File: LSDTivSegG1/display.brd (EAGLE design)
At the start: 150 x 100 mm, 99 parts, among them IC1 MEGA8-P, IC2 MAX232, IC3 PCF8574P, IC4 PCF8574P, IC5 PCF8574P, IC6 PCF8574P

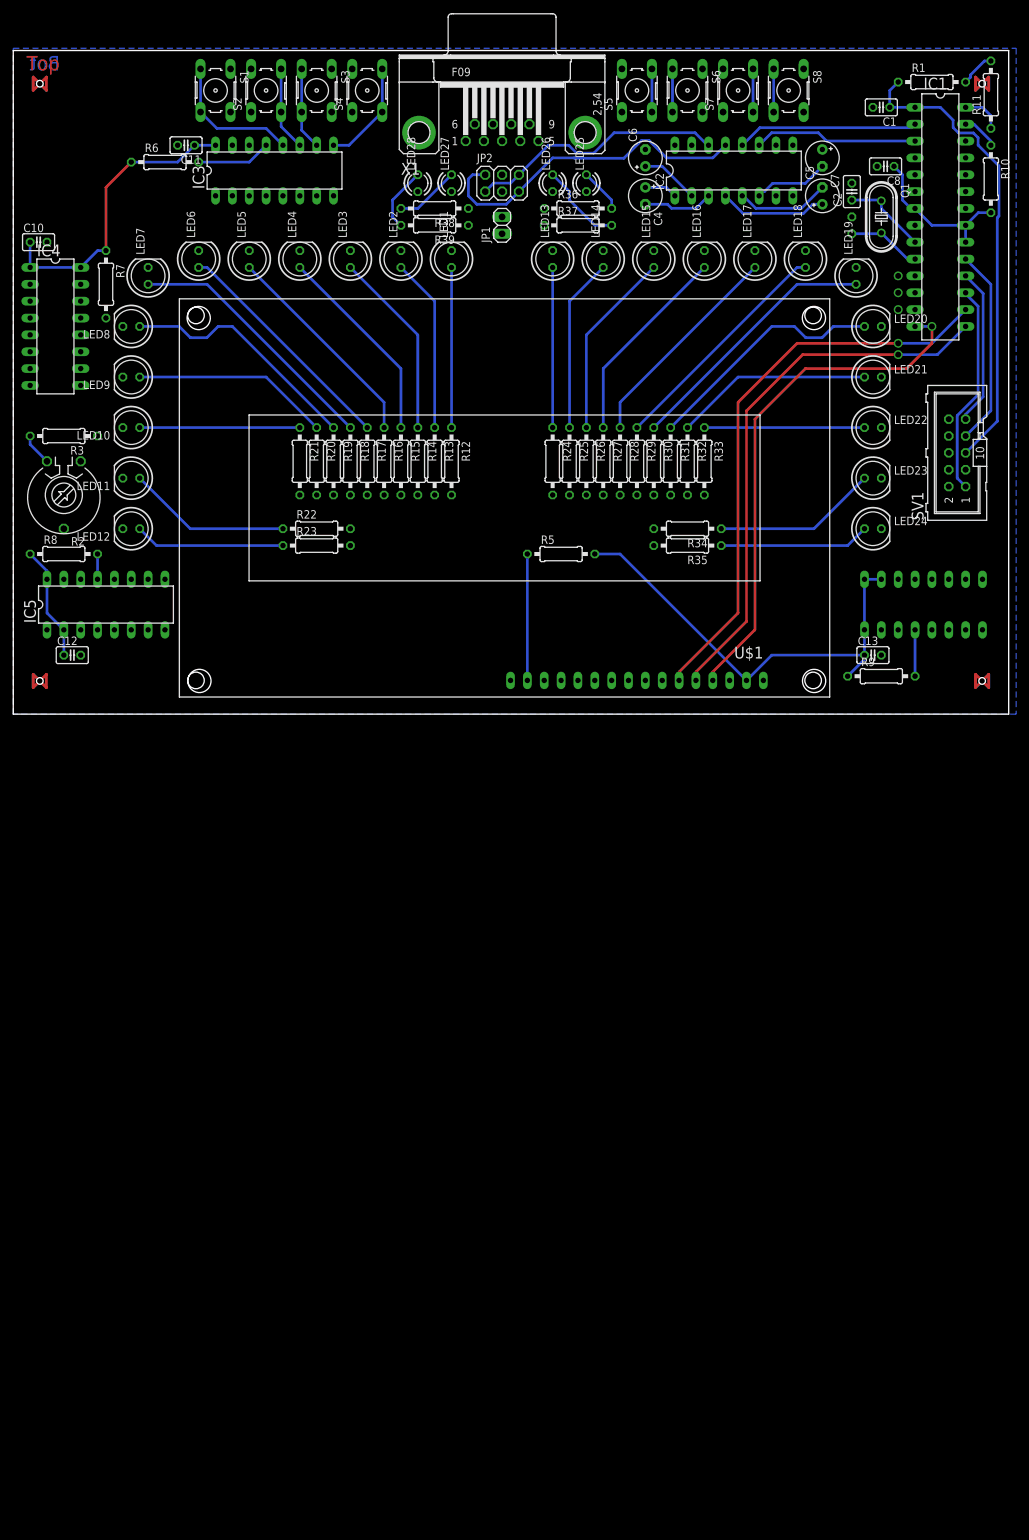
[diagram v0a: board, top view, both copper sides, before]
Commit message: worked on board layout (ca. 80% routed) changed LEDs from GND to +5V
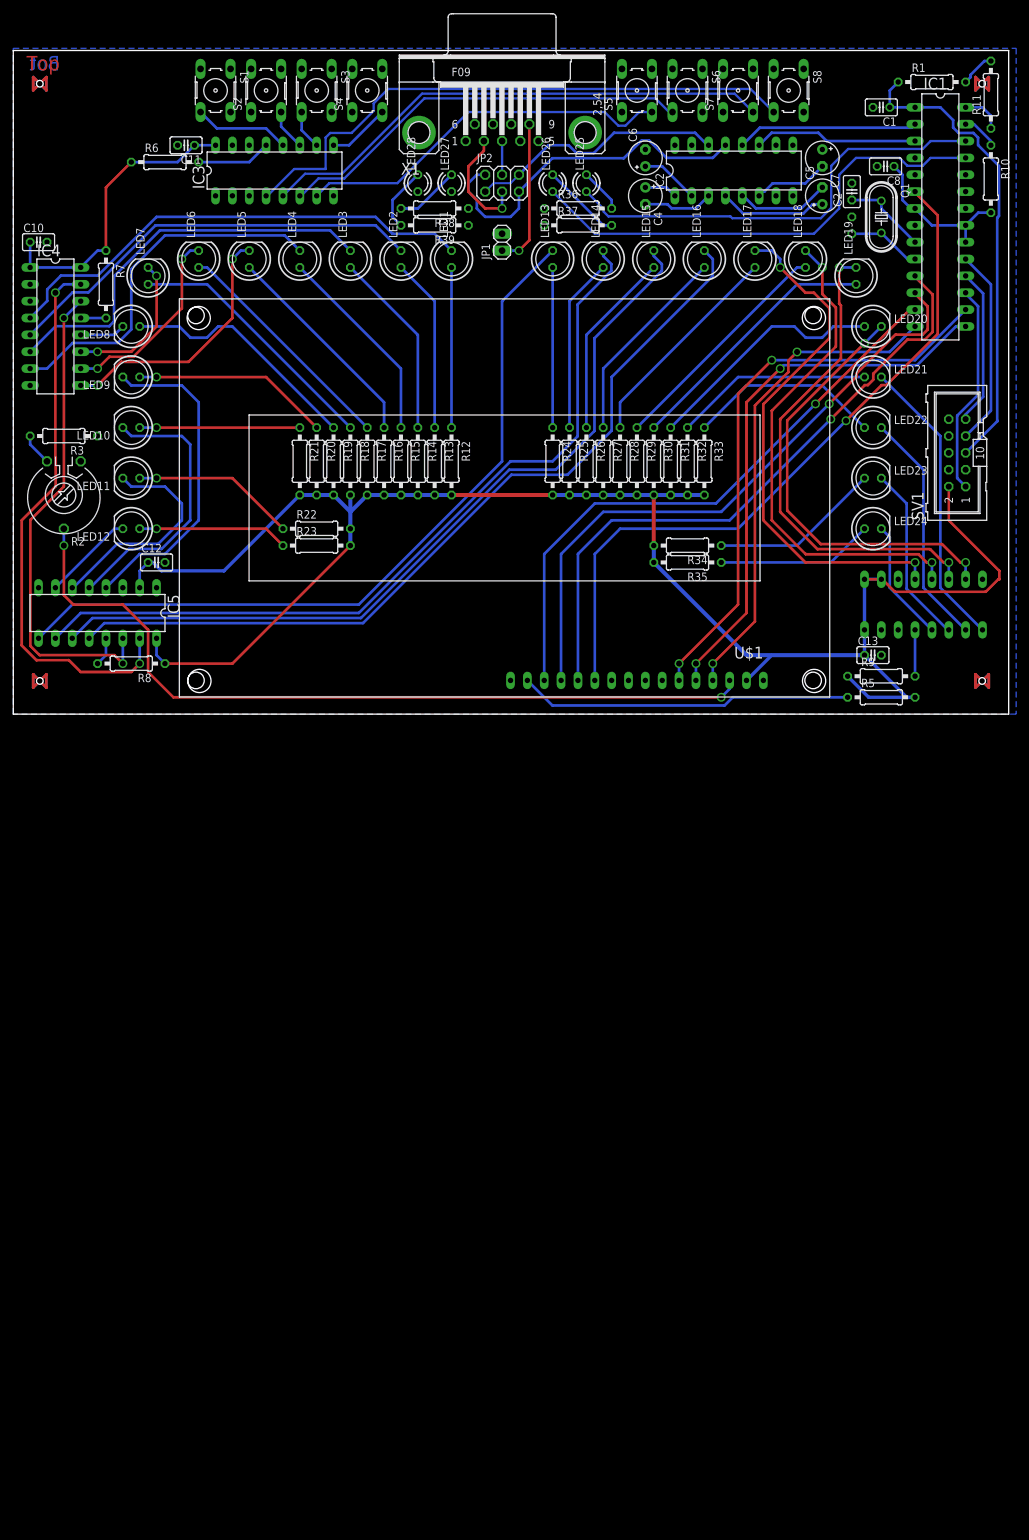
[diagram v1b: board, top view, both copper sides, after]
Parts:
- moved R5 52.9 mm to (130.8, 2.54)
- moved R8 19.4 mm to (17.8, 7.62), turned to 180 degrees
- moved C12 18.9 mm to (21.6, 22.9)
- moved R34 2.54 mm to (101.6, 25.4)
- moved R35 2.54 mm to (101.6, 22.9)
- moved JP1 2.54 mm to (73.7, 71.1)
- moved IC5 1.80 mm to (12.7, 15.2), turned to 180 degrees
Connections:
- net +5V: now also R12.2, R13.2, R14.2, R15.2, R16.2, R17.2, R18.2, R19.2, R20.2, R21.2, R22.2, R23.2, R24.2, R25.2, R26.2, R27.2, R28.2, R29.2, R30.2, R31.2, R32.2, R33.2, R34.2, R35.2
- net GND: no longer R12.2, R13.2, R14.2, R15.2, R16.2, R17.2, R18.2, R19.2, R20.2, R21.2, R22.2, R23.2, R24.2, R25.2, R26.2, R27.2, R28.2, R29.2, R30.2, R31.2, R32.2, R33.2, R34.2, R35.2
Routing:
- net +5V: track 159.8 -> 358.7 mm
- net LED15: track 0.00 -> 125.7 mm
- net LED14: track 0.00 -> 123.5 mm
- net N$10: track 0.00 -> 122.2 mm, vias 0 -> 2
- net LED13: track 0.00 -> 121.9 mm
- net LED12: track 0.00 -> 115.8 mm
- net D4: track 0.00 -> 107.3 mm, vias 0 -> 1
- net D5: track 0.00 -> 96.4 mm, vias 0 -> 1
- net D6: track 0.00 -> 94.9 mm, vias 0 -> 1
- net D7: track 0.00 -> 90.2 mm, vias 0 -> 1
- net SDA: track 6.13 -> 89.5 mm, vias 0 -> 2
- net BTN0: track 6.50 -> 88.0 mm
- net LED16: track 0.00 -> 79.7 mm, vias 0 -> 2
- net LED17: track 0.00 -> 75.8 mm, vias 0 -> 2
- net LED18: track 0.00 -> 74.4 mm, vias 0 -> 2
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
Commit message: added npn transistors to LED bars
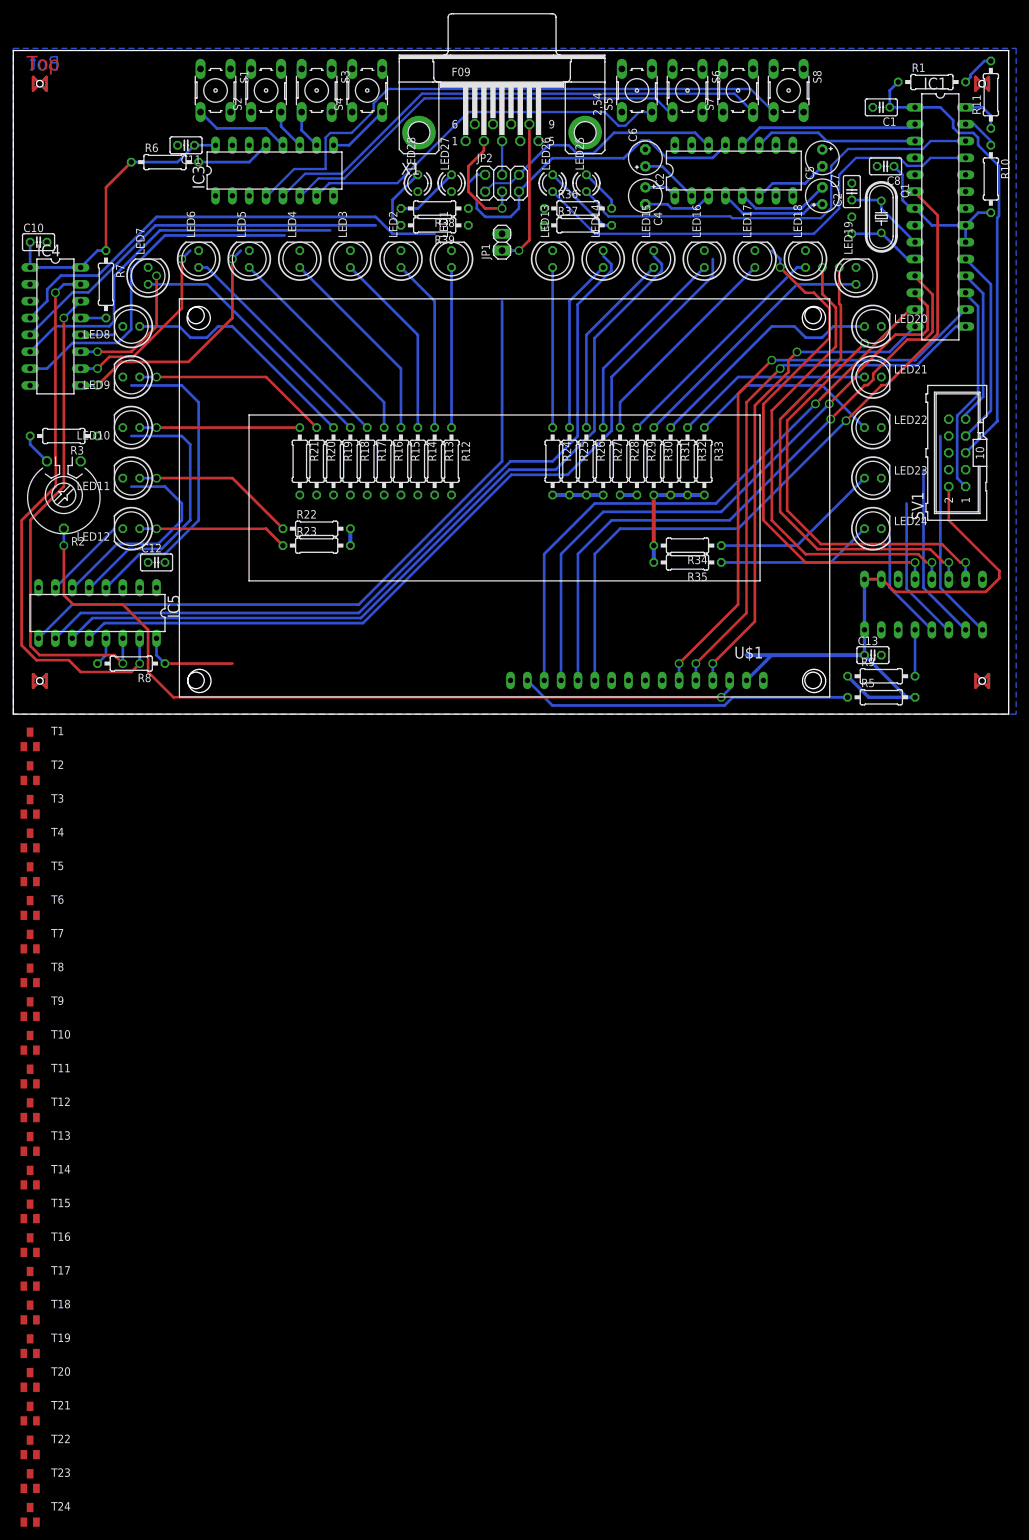
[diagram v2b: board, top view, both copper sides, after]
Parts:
- added T1, T10, T11, T12, T13, T14, T15, T16, T17, T18, T19, T2, T20, T21, T22, T23, T24, T3, T4, T5, T6, T7, T8, T9: BC847, transistor:SOT23
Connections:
- new net N$51: LED9.K, T9.3
- new net N$53: LED1.K, T1.3
- new net N$54: LED2.K, T2.3
- new net N$55: LED3.K, T3.3
- new net N$56: LED4.K, T4.3
- new net N$57: LED5.K, T5.3
- new net N$58: LED6.K, T6.3
- new net N$59: LED17.K, T17.3
- new net N$60: LED10.K, T10.3
- new net N$61: LED11.K, T11.3
- new net N$62: LED12.K, T12.3
- new net N$63: LED13.K, T13.3
- new net N$64: LED14.K, T14.3
- new net N$65: LED7.K, T7.3
- new net N$66: LED8.K, T8.3
- new net N$67: LED15.K, T15.3
- new net N$68: LED16.K, T16.3
- new net N$69: LED18.K, T18.3
- new net N$70: LED19.K, T19.3
- new net N$71: LED20.K, T20.3
- new net N$72: LED21.K, T21.3
- new net N$73: LED22.K, T22.3
- new net N$74: LED23.K, T23.3
- new net N$75: LED24.K, T24.3
- net GND: now also T1.2, T10.2, T11.2, T12.2, T13.2, T14.2, T15.2, T16.2, T17.2, T18.2, T19.2, T2.2, T20.2, T21.2, T22.2, T23.2, T24.2, T3.2, T4.2, T5.2, T6.2, T7.2, T8.2, T9.2
- net LED0: now also T1.1; no longer LED1.K
- net LED1: now also T2.1; no longer LED2.K
- net LED10: now also T11.1; no longer LED11.K
- net LED11: now also T12.1; no longer LED12.K
- net LED12: now also T13.1; no longer LED13.K
- net LED13: now also T14.1; no longer LED14.K
- net LED14: now also T15.1; no longer LED15.K
- net LED15: now also T16.1; no longer LED16.K
- net LED16: now also T17.1; no longer LED17.K
- net LED17: now also T18.1; no longer LED18.K
- net LED18: now also T19.1; no longer LED19.K
- net LED19: now also T20.1; no longer LED20.K
- net LED2: now also T3.1; no longer LED3.K
- net LED20: now also T21.1; no longer LED21.K
- net LED21: now also T22.1; no longer LED22.K
- net LED22: now also T23.1; no longer LED23.K
- net LED23: now also T24.1; no longer LED24.K
- net LED3: now also T4.1; no longer LED4.K
- net LED4: now also T5.1; no longer LED5.K
- net LED5: now also T6.1; no longer LED6.K
- net LED6: now also T7.1; no longer LED7.K
- net LED7: now also T8.1; no longer LED8.K
- net LED8: now also T9.1; no longer LED9.K
- net LED9: now also T10.1; no longer LED10.K
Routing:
- net +5V: track 358.7 -> 230.9 mm
- net LED20: track 44.4 -> 31.8 mm
- net LED12: track 115.8 -> 105.0 mm
- net LED21: track 35.7 -> 26.8 mm
- net LED22: track 27.2 -> 21.8 mm
- net LED1: track 64.3 -> 58.9 mm
- net LED2: track 61.1 -> 56.8 mm
- net LED0: track 72.9 -> 69.3 mm
- net LED19: track 66.3 -> 62.7 mm
- net LED17: track 75.8 -> 72.2 mm
- net LED3: track 55.2 -> 52.0 mm
- net LED18: track 74.4 -> 71.8 mm
- net LED16: track 79.7 -> 77.2 mm
- net LED23: track 18.4 -> 16.6 mm
- net LED9: track 42.1 -> 40.3 mm
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
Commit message: routed led transistors
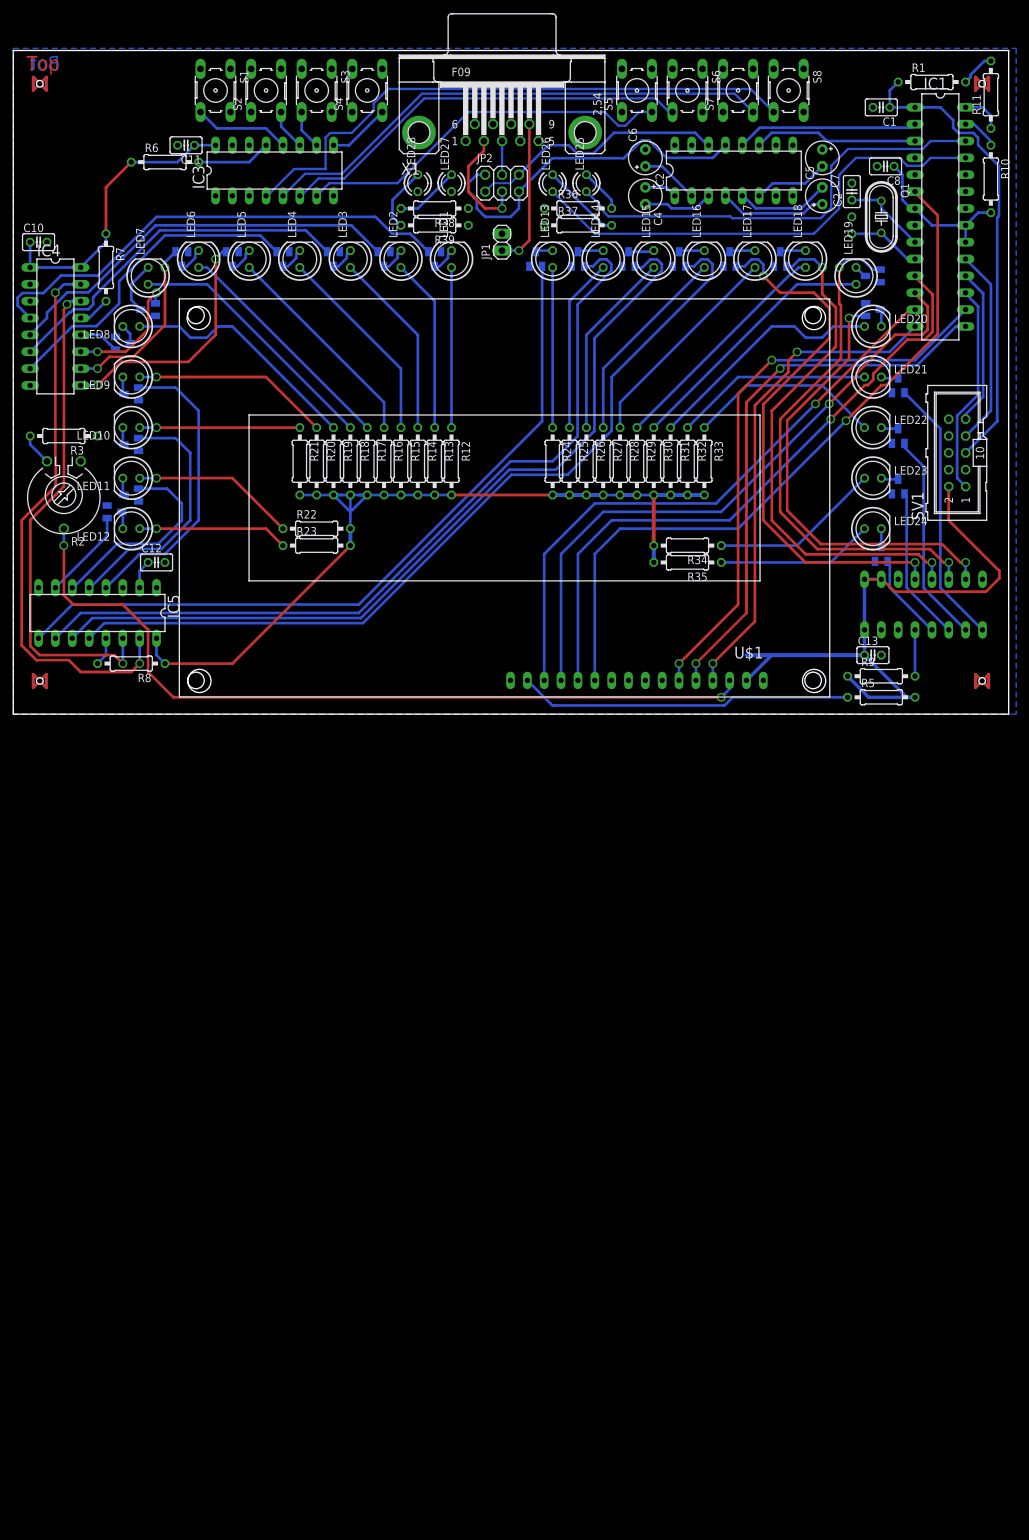
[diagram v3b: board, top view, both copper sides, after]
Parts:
- moved T19 205.3 mm to (129.5, 66.0), flipped to the bottom, turned to 270 degrees
- moved T20 205.3 mm to (129.5, 61.0), flipped to the bottom, turned to 90 degrees
- moved T21 202.8 mm to (133.3, 49.5), flipped to the bottom
- moved T22 200.8 mm to (133.3, 41.9), flipped to the bottom
- moved T23 198.9 mm to (133.3, 34.3), flipped to the bottom
- moved T18 194.9 mm to (115.6, 68.6), flipped to the bottom
- moved T24 193.4 mm to (130.8, 24.1), flipped to the bottom
- moved T17 186.3 mm to (108.0, 68.6), flipped to the bottom
- moved T16 177.9 mm to (100.3, 68.6), flipped to the bottom
- moved T15 169.5 mm to (92.7, 68.6), flipped to the bottom
- moved T14 161.2 mm to (85.1, 68.6), flipped to the bottom
- moved T13 153.6 mm to (78.7, 68.6), flipped to the bottom
- moved T6 100.4 mm to (25.4, 68.6), flipped to the bottom, turned to 180 degrees
- moved T5 97.6 mm to (33.0, 68.6), flipped to the bottom, turned to 180 degrees
- moved T7 96.9 mm to (20.3, 61.0), flipped to the bottom, turned to 270 degrees
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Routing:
- net +5V: track 230.9 -> 317.6 mm
- net LED20: track 31.8 -> 40.6 mm
- net N$65: track 0.00 -> 8.00 mm
- net LED12: track 105.0 -> 112.8 mm
- net LED18: track 71.8 -> 79.1 mm
- net LED17: track 72.2 -> 78.6 mm
- net LED16: track 77.2 -> 82.7 mm
- net LED19: track 62.7 -> 68.2 mm
- net LED21: track 26.8 -> 31.9 mm
- net LED15: track 123.9 -> 127.9 mm
- net N$67: track 0.00 -> 3.88 mm
- net N$69: track 0.00 -> 3.88 mm
- net N$68: track 0.00 -> 3.88 mm
- net N$64: track 0.00 -> 3.88 mm
- net N$59: track 0.00 -> 3.88 mm
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
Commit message: worked on dispaly.brd, only some airwire left
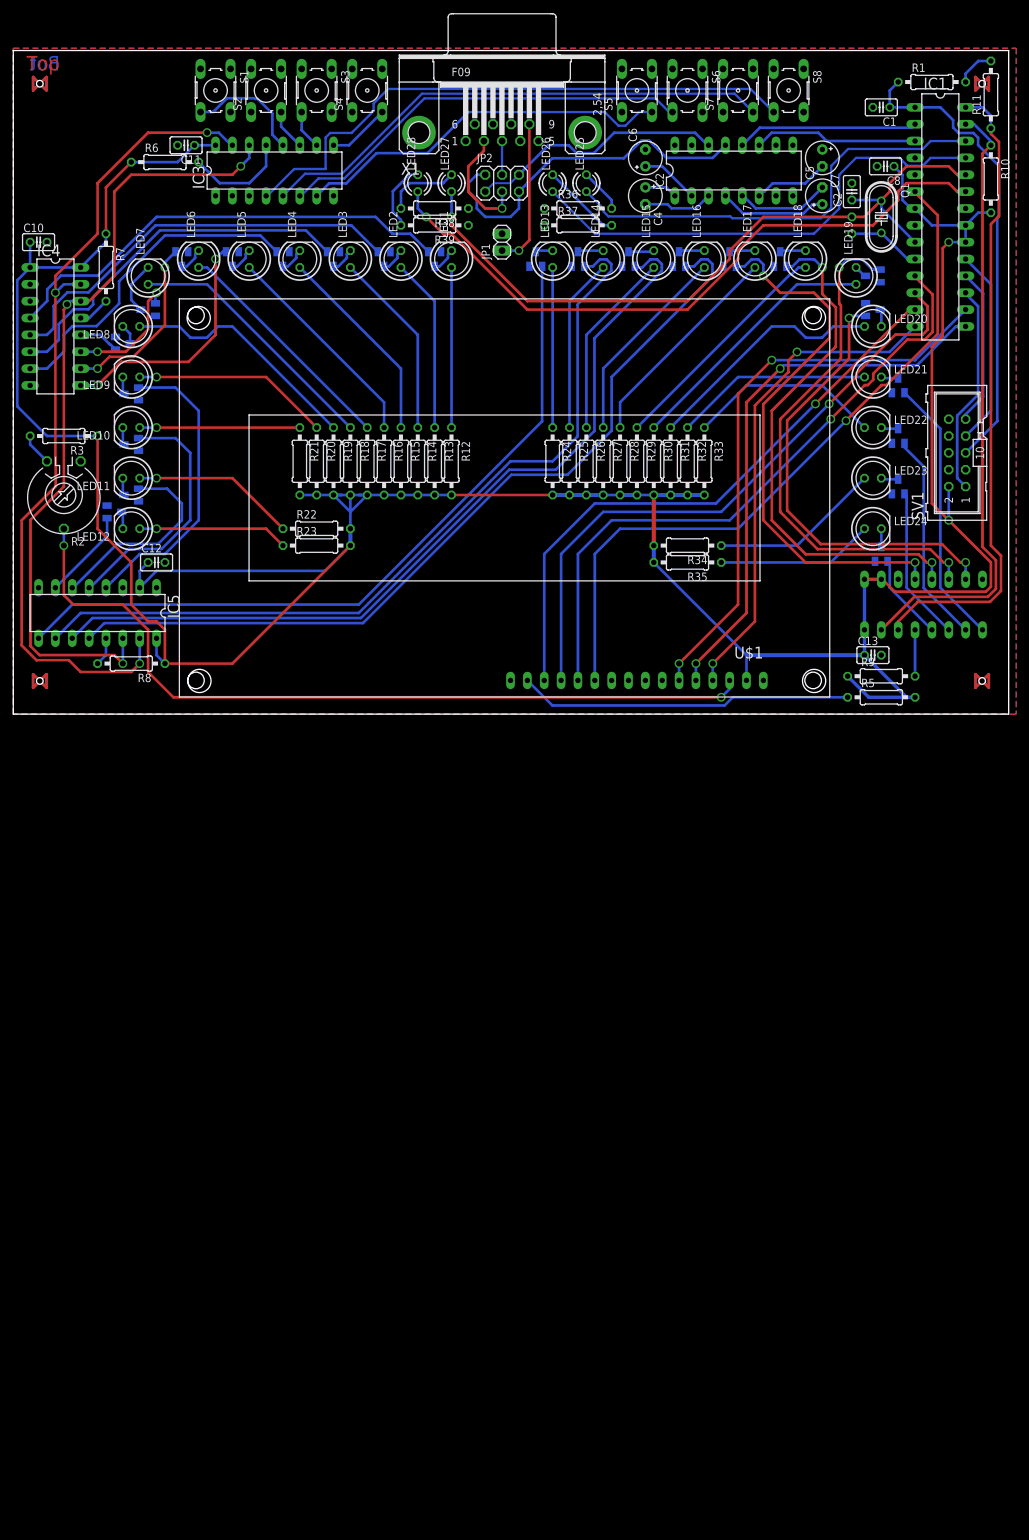
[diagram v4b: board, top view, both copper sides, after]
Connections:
- removed net SDL: IC3.14, IC4.14, IC5.14, IC6.14
- net SCL: now also IC3.14, IC4.14, IC5.14, IC6.14
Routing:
- net SCL: track 7.51 -> 214.2 mm, vias 0 -> 3
- net +5V: track 317.6 -> 491.1 mm, vias 0 -> 2
- net SDA: track 89.5 -> 221.0 mm, vias 2 -> 3
- net N$40: track 0.00 -> 101.3 mm, vias 0 -> 1
- net N$41: track 0.00 -> 97.7 mm, vias 0 -> 1
- net SDL: track 74.9 -> 0.00 mm, vias 2 -> 0
- net N$12: track 11.2 -> 15.7 mm
- net BTN7: track 14.5 -> 18.1 mm
- net LED0: track 72.9 -> 69.5 mm
- net LED2: track 54.3 -> 55.9 mm
- net LED1: track 61.3 -> 62.8 mm
- net N$45: track 9.72 -> 11.2 mm
- net LED3: track 48.4 -> 49.9 mm
- net N$44: track 9.72 -> 10.4 mm
- added copper zone on layer 1, net GND
